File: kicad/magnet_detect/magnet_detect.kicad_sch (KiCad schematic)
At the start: 8 parts, among them J1 Conn_01x06_Socket, U1 AS5047D

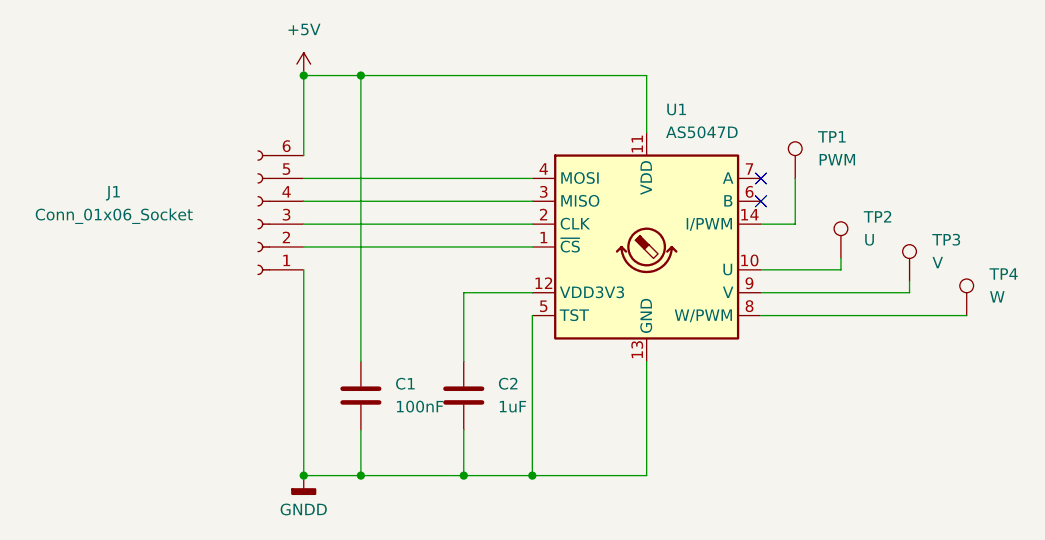
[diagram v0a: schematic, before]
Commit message: fix(kicad):esp32_magnet
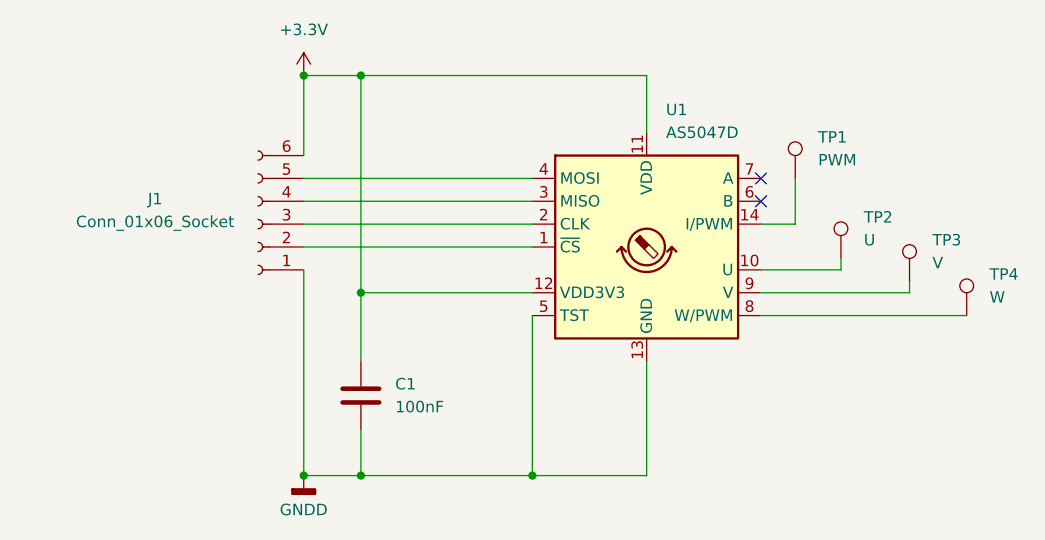
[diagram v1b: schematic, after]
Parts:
- removed C2: 1uF, Capacitor_SMD:C_0603_1608Metric, symbol Device:C
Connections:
- net +5V is gone; now on net +3.3V: C1.1, J1.6 (Pin_6), U1.11 (VDD)
- net +3.3V: now reaches U1.12 (VDD3V3)
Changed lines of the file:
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@@
+	)
+	(junction
+		(at 74.93 76.2)
+		(diameter 0)
+		(color 0 0 0 0)
 	)
 	(junction
@@
 	)
 	(junction
-		(at 92.71 120.65)
+		(at 81.28 100.33)
 		(diameter 0)
 		(color 0 0 0 0)
 	)
-	(junction
-		(at 74.93 76.2)
-		(diameter 0)
-		(color 0 0 0 0)
-	)
 	(no_connect
 		(at 125.73 90.17)
@@
 	(wire
 		(pts
+			(xy 81.28 100.33) (xy 100.33 100.33)
+		)
+		(stroke
+			(width 0)
+			(type default)
+		)
+	)
+	(wire
+		(pts
 			(xy 81.28 115.57) (xy 81.28 120.65)
 		)
@@
 	(wire
 		(pts
+			(xy 81.28 100.33) (xy 81.28 107.95)
+		)
+		(stroke
+			(width 0)
+			(type default)
+		)
+	)
+	(wire
+		(pts
 			(xy 81.28 76.2) (xy 74.93 76.2)
 		)
@@
 	(wire
 		(pts
-			(xy 81.28 76.2) (xy 81.28 107.95)
+			(xy 81.28 76.2) (xy 81.28 100.33)
 		)
 		(stroke
@@
 	(wire
 		(pts
-			(xy 92.71 115.57) (xy 92.71 120.65)
-		)
-		(stroke
-			(width 0)
-			(type default)
-		)
-	)
-	(wire
-		(pts
 			(xy 134.62 97.79) (xy 134.62 96.52)
 		)
@@
 	(wire
 		(pts
-			(xy 81.28 120.65) (xy 92.71 120.65)
-		)
-		(stroke
-			(width 0)
-			(type default)
-		)
-	)
-	(wire
-		(pts
-			(xy 92.71 120.65) (xy 100.33 120.65)
-		)
-		(stroke
-			(width 0)
-			(type default)
-		)
-	)
-	(wire
-		(pts
-			(xy 92.71 107.95) (xy 92.71 100.33)
+			(xy 81.28 120.65) (xy 100.33 120.65)
 		)
 		(stroke
@@
 		(pts
 			(xy 74.93 95.25) (xy 100.33 95.25)
-		)
-		(stroke
-			(width 0)
-			(type default)
-		)
-	)
-	(wire
-		(pts
-			(xy 92.71 100.33) (xy 100.33 100.33)
 		)
 		(stroke
@@
 		(dnp no)
 		(property "Reference" "J1"
-			(at 53.848 89.154 0)
+			(at 58.42 89.916 0)
 			(effects
 				(font
@@
 		)
 		(property "Value" "Conn_01x06_Socket"
-			(at 53.848 91.694 0)
+			(at 58.42 92.456 0)
 			(effects
 				(font
@@
 				(path "/c3e2cd2e-47db-48d7-8ae5-f0c1ce0b1bef"
 					(reference "J1")
-					(unit 1)
-				)
-			)
-		)
-	)
-	(symbol
-		(lib_id "power:+5V")
-		(at 74.93 76.2 0)
-		(unit 1)
-		(exclude_from_sim no)
-		(in_bom yes)
-		(on_board yes)
-		(dnp no)
-		(fields_autoplaced yes)
-		(property "Reference" "#PWR02"
-			(at 74.93 80.01 0)
-			(effects
-				(font
-					(size 1.27 1.27)
-				)
-				(hide yes)
-			)
-		)
-		(property "Value" "+5V"
-			(at 74.93 71.12 0)
-			(effects
-				(font
-					(size 1.27 1.27)
-				)
-			)
-		)
-		(property "Footprint" ""
-			(at 74.93 76.2 0)
-			(effects
-				(font
-					(size 1.27 1.27)
-				)
-				(hide yes)
-			)
-		)
-		(property "Datasheet" ""
-			(at 74.93 76.2 0)
-			(effects
-				(font
-					(size 1.27 1.27)
-				)
-				(hide yes)
-			)
-		)
-		(property "Description" "Power symbol creates a global label with name \"+5V\""
-			(at 74.93 76.2 0)
-			(effects
-				(font
-					(size 1.27 1.27)
-				)
-				(hide yes)
-			)
-		)
-		(pin "1"
-		)
-		(instances
-			(project ""
-				(path "/c3e2cd2e-47db-48d7-8ae5-f0c1ce0b1bef"
-					(reference "#PWR02")
 					(unit 1)
 				)
@@
 	)
 	(symbol
-		(lib_id "Device:C")
-		(at 92.71 111.76 0)
-		(unit 1)
-		(exclude_from_sim no)
-		(in_bom yes)
-		(on_board yes)
-		(dnp no)
-		(fields_autoplaced yes)
-		(property "Reference" "C2"
-			(at 96.52 110.4899 0)
-			(effects
-				(font
-					(size 1.27 1.27)
-				)
-				(justify left)
-			)
-		)
-		(property "Value" "1uF"
-			(at 96.52 113.0299 0)
-			(effects
-				(font
-					(size 1.27 1.27)
-				)
-				(justify left)
-			)
-		)
-		(property "Footprint" "Capacitor_SMD:C_0603_1608Metric"
-			(at 93.6752 115.57 0)
-			(effects
-				(font
-					(size 1.27 1.27)
-				)
-				(hide yes)
-			)
-		)
-		(property "Datasheet" "~"
-			(at 92.71 111.76 0)
-			(effects
-				(font
-					(size 1.27 1.27)
-				)
-				(hide yes)
-			)
-		)
-		(property "Description" "Unpolarized capacitor"
-			(at 92.71 111.76 0)
-			(effects
-				(font
-					(size 1.27 1.27)
-				)
-				(hide yes)
-			)
-		)
-		(pin "2"
-		)
-		(pin "1"
-		)
-		(instances
-			(project "magnet_detect"
-				(path "/c3e2cd2e-47db-48d7-8ae5-f0c1ce0b1bef"
-					(reference "C2")
-					(unit 1)
-				)
-			)
-		)
-	)
-	(symbol
 		(lib_id "Connector:TestPoint")
 		(at 134.62 96.52 0)
@@
 					(unit 1)
 				)
+			)
+		)
+	)
+	(symbol
+		(lib_id "power:+3.3V")
+		(at 74.93 76.2 0)
+		(unit 1)
+		(exclude_from_sim no)
+		(in_bom yes)
+		(on_board yes)
+		(dnp no)
+		(fields_autoplaced yes)
+		(property "Reference" "#PWR02"
+			(at 74.93 80.01 0)
+			(effects
+				(font
+					(size 1.27 1.27)
+				)
+				(hide yes)
+			)
+		)
+		(property "Value" "+3.3V"
+			(at 74.93 71.12 0)
+			(effects
+				(font
+					(size 1.27 1.27)
+				)
+			)
+		)
+		(property "Footprint" ""
+			(at 74.93 76.2 0)
+			(effects
+				(font
+					(size 1.27 1.27)
+				)
+				(hide yes)
+			)
+		)
+		(property "Datasheet" ""
+			(at 74.93 76.2 0)
+			(effects
+				(font
+					(size 1.27 1.27)
+				)
+				(hide yes)
+			)
+		)
+		(property "Description" "Power symbol creates a global label with name \"+3.3V\""
+			(at 74.93 76.2 0)
+			(effects
+				(font
+					(size 1.27 1.27)
+				)
+				(hide yes)
+			)
+		)
+		(pin "1"
+		)
+		(instances
+			(project ""
+				(path "/c3e2cd2e-47db-48d7-8ae5-f0c1ce0b1bef"
+					(reference "#PWR02")
+					(unit 1)
+				)
